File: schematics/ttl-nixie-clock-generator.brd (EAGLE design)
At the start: 100 x 80 mm, 13 parts, among them IC1 7400N, Q1 1MHz

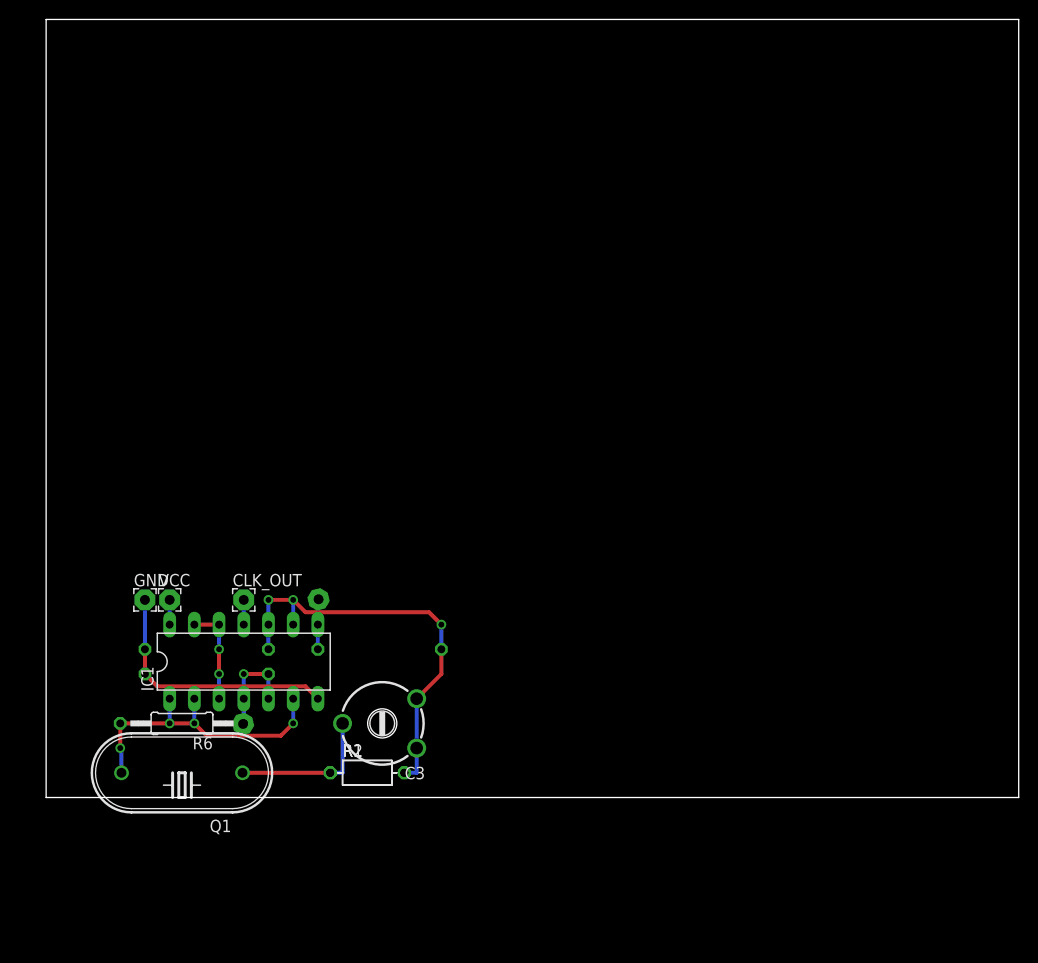
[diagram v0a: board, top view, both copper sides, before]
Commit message: ttl-generator: protoboard built version
The version i built on protoboard, it works!
The multimeter says 999.7 kHz :)
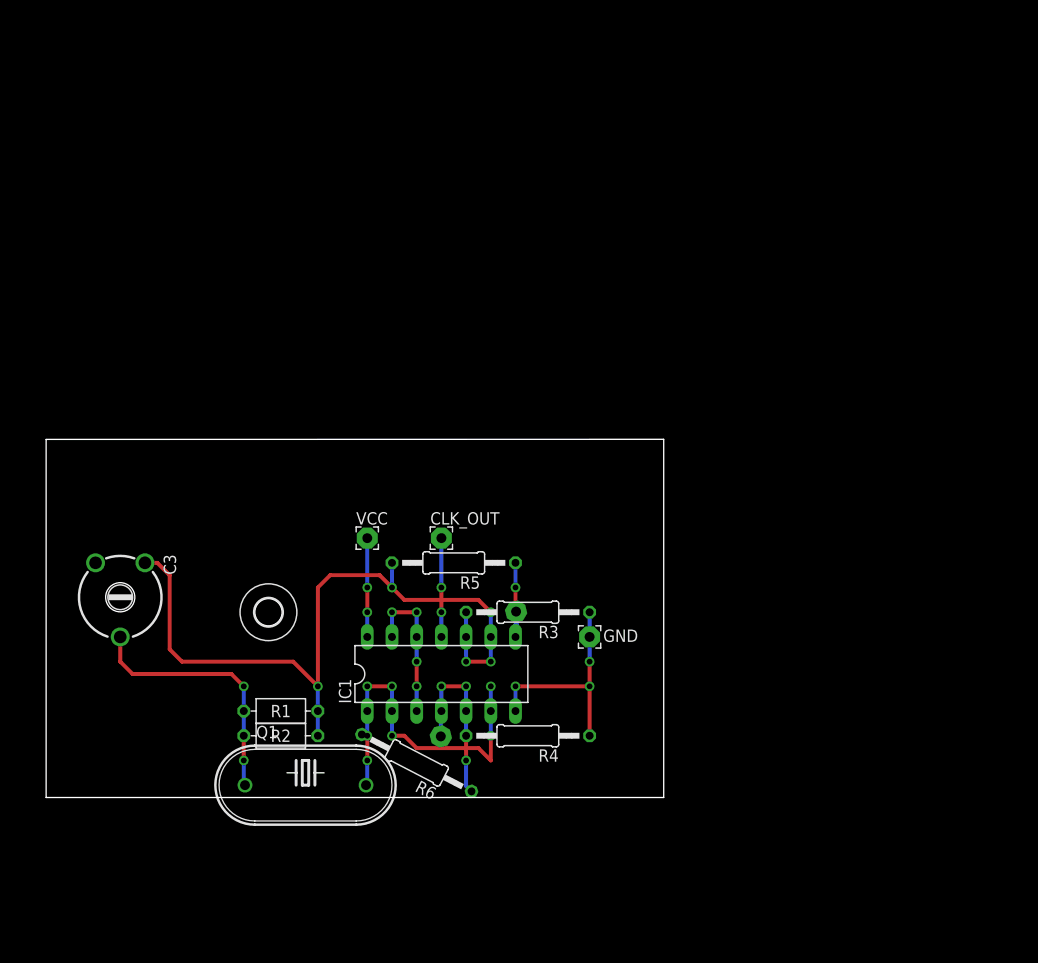
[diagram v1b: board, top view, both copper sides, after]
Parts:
- added U$1: (no value), holes:2,8
- CLK_OUT: value (none) -> CLK_OUT
- GND: value (none) -> GND
- VCC: value (none) -> VCC
- moved GND 45.9 mm to (55.9, 16.5)
- moved R4 33.6 mm to (49.5, 6.35), flipped to the top
- moved R3 33.2 mm to (49.5, 19.1), flipped to the top
- moved C3 31.2 mm to (7.62, 21.6), turned to 180 degrees
- moved R6 24.5 mm to (38.1, 3.56), turned to 152.6 degrees
- moved VCC 21.3 mm to (33.0, 26.7)
- moved CLK_OUT 21.3 mm to (40.6, 26.7)
- moved C2 20.4 mm to (44.5, 12.7), turned to 301.1 degrees
- moved IC1 20.4 mm to (40.6, 12.7)
- moved Q1 12.8 mm to (26.7, 1.27), turned to 0 degrees
- moved R5 11.7 mm to (41.9, 24.1), flipped to the top
- moved R1 10.9 mm to (24.1, 8.89)
- moved R2 9.67 mm to (24.1, 6.35)
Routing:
- net N$2: track 44.0 -> 77.9 mm, vias 4 -> 5
- net N$1: track 15.4 -> 26.5 mm, vias 0 -> 2
- net N$6: track 31.6 -> 39.8 mm, vias 4 -> 7
- net VCC: track 2.54 -> 10.2 mm, vias 0 -> 2
- net CLK_OUT: track 2.54 -> 10.2 mm, vias 0 -> 2
- net N$5: track 12.8 -> 18.7 mm, vias 3 -> 4
- net N$3: track 10.2 -> 15.2 mm, vias 2 -> 4
- net N$4: track 5.17 -> 9.98 mm, vias 0 -> 2
- net GND: track 26.5 -> 22.9 mm, vias 0 -> 3
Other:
- board size 100 x 80 mm -> 63.5 x 36.8 mm

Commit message: nixie-clock-generator: added divide circuit, prettify
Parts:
- added CLK_1HZ: VCC, wirepad:2,15/1,0
- added IC2, IC3, IC4, IC5, IC6, IC8: 74LS93N, 74xx-eu:DIL14
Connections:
- removed net CLK_OUT: CLK_OUT.1, IC1.11
- new net CLK_1HZ: CLK_1HZ.1, IC8.11, IC8.2
- new net CLK_1MHZ: CLK_OUT.1, IC1.11, IC2.14
- new net N$10: IC5.11, IC5.2, IC6.14
- new net N$11: IC6.1, IC6.12
- new net N$12: IC6.3, IC6.9
- new net N$13: IC6.11, IC6.2, IC8.14
- new net N$14: IC8.1, IC8.12
- new net N$15: IC8.3, IC8.9
- new net N$16: IC2.1, IC2.12
- new net N$17: IC2.11, IC2.2, IC3.14
- new net N$18: IC2.3, IC2.9
- new net N$19: IC3.3, IC3.9
- new net N$20: IC3.11, IC3.2, IC4.14
- new net N$21: IC3.1, IC3.12
- new net N$22: IC4.1, IC4.12
- new net N$23: IC4.3, IC4.9
- new net N$24: IC4.11, IC4.2, IC5.14
- new net N$8: IC5.1, IC5.12
- new net N$9: IC5.3, IC5.9
- net GND: now also IC2.10, IC3.10, IC4.10, IC5.10, IC6.10, IC8.10
- net VCC: now also IC2.5, IC3.5, IC4.5, IC5.5, IC6.5, IC8.5
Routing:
- net GND: track 22.9 -> 224.5 mm
- net VCC: track 10.2 -> 140.8 mm, vias 2 -> 3
- net CLK_1MHZ: track 0.00 -> 95.1 mm, vias 0 -> 2
- net N$24: track 0.00 -> 32.9 mm
- net N$20: track 0.00 -> 32.9 mm
- net N$17: track 0.00 -> 32.9 mm
- net N$10: track 0.00 -> 32.9 mm
- net N$13: track 0.00 -> 32.9 mm
- net CLK_1HZ: track 0.00 -> 16.1 mm
- net N$23: track 0.00 -> 12.3 mm
- net N$19: track 0.00 -> 12.3 mm
- net N$18: track 0.00 -> 12.3 mm
- net N$12: track 0.00 -> 12.3 mm
- net N$9: track 0.00 -> 12.3 mm
- net N$15: track 0.00 -> 12.3 mm
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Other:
- board text added: "we're constructing only the 1MHz generator (the board contents) the divider circuit added just for the referece"
